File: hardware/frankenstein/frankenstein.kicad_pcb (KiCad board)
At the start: 2 copper layers, 100 x 99.9 mm, 259 parts, among them J351 MINI-USB-5P-3400020P1, M200 CONN_1, M201 CONN_1, M202 CONN_1, M351 CONN_1, M352 CONN_1, M401 CONN_1, M470 CONN_1, M471 CONN_1, P104 CONN_4, P201 CONN_10X2, P202 CONN_3, P203 CONN_2, P204 CONN_1, P205 CONN_1, P208 CONN_6, P209 CONN_6, P351 CONN_5X2, P352 MICRO-SDCARD-CONNECTOR-330006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, P353 CONN_10X2, P356 CONN_1, P401 CONN_3, P402 CONN_10X2, P403 CONN_16, P404 CONN_1, P405 CONN_1, P472 CONN_2, P51 CONN_4X2, P52 CONN_10X2, P53 CONN_2, P54 CONN_5X2, P55 CONN_6, P56 CONN_6, P57 CONN_6, P58 CONN_6, P603 CONN_6, P610 CONN_1, Q401 OVP_DRIVER, Q402 OVP_DRIVER, Q403 OVP_DRIVER, Q404 OVP_DRIVER, Q405 OVP_DRIVER, Q406 OVP_DRIVER, Q407 OVP_DRIVER, Q408 OVP_DRIVER, Q409 OVP_DRIVER, Q410 OVP_DRIVER, Q411 OVP_DRIVER, Q412 OVP_DRIVER, U101 MAX9926/9927, U201 LMV324IDR, U202 LMV324IDR, U203 LMV324IDR, U351 FT232RL, U471 SN65HVD230, U601 TC4427AVOA, U602 TC4427AVOA, U603 TC4427AVOA

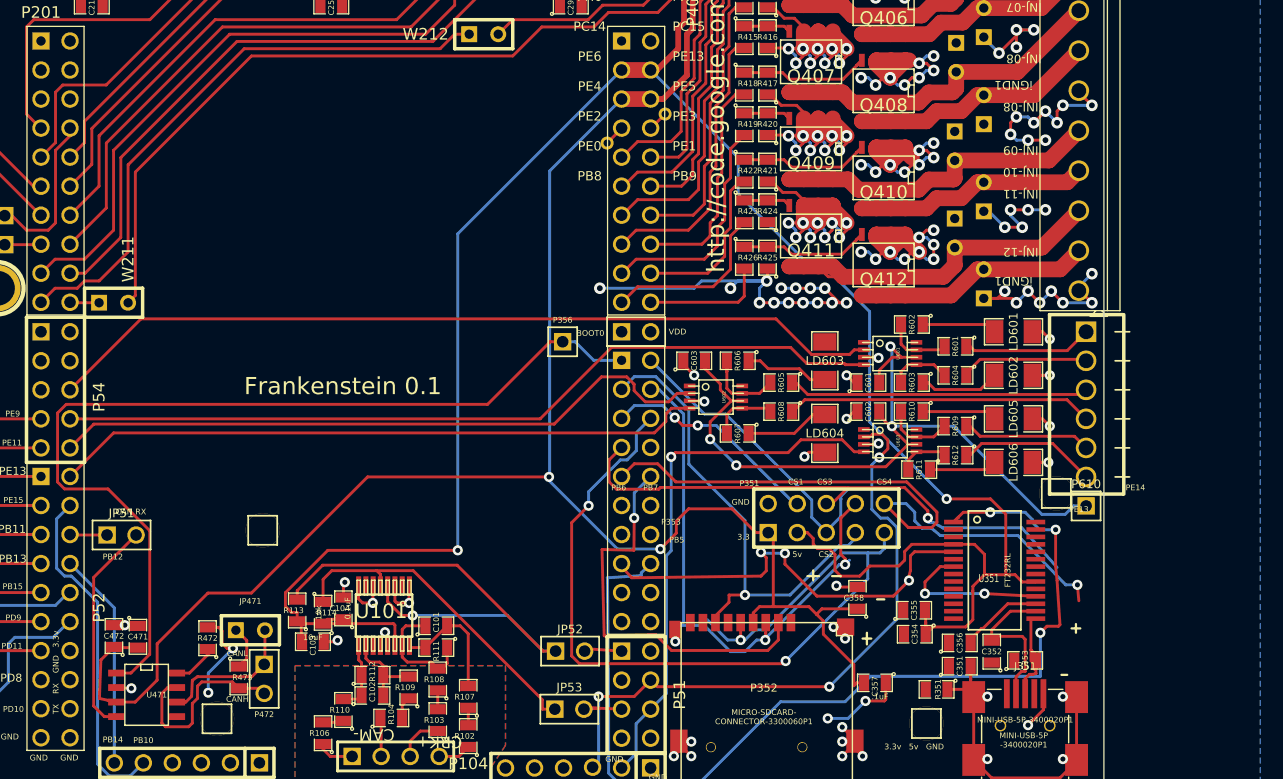
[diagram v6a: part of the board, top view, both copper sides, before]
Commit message: MSOP >> SOIC
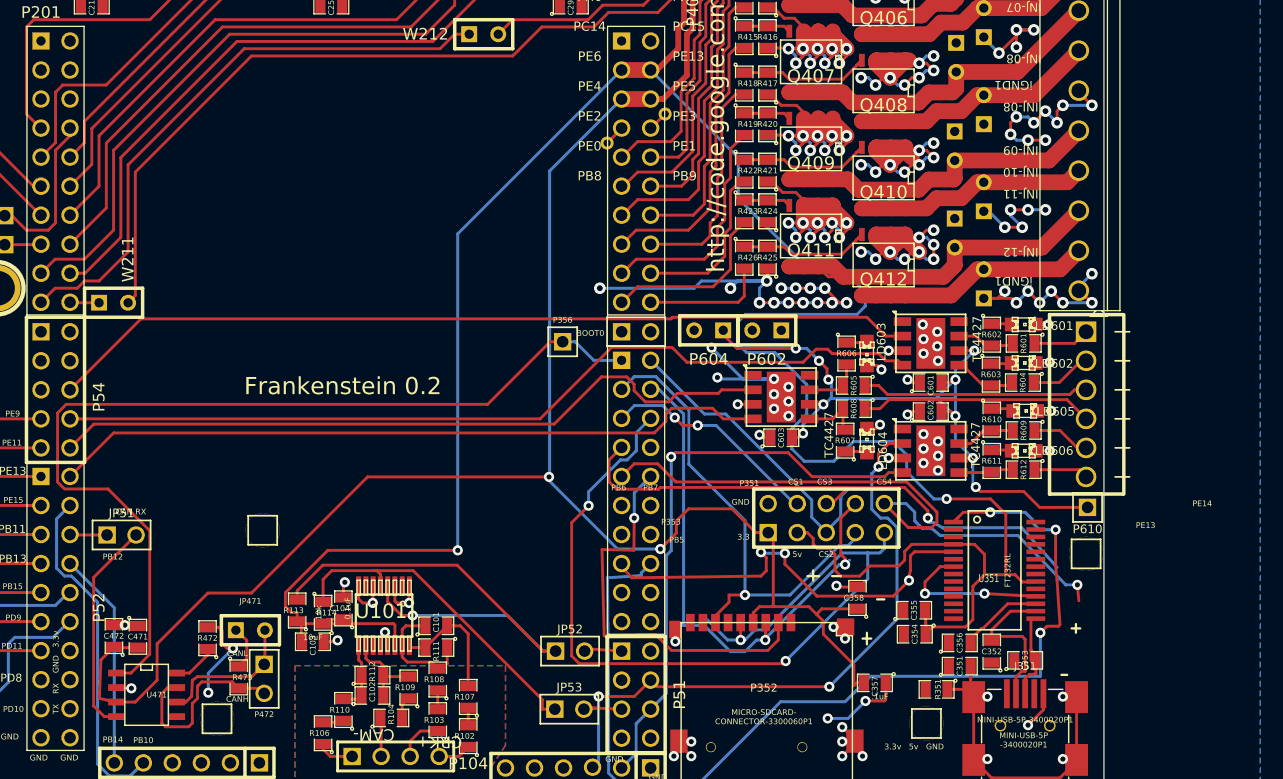
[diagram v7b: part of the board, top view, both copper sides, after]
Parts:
- added P602: CONN_2, SIL-2, F.Cu at (190.5, 152.3)
- added P604: CONN_2, SIL-2, F.Cu at (185.4, 152.3)
- LD601, LD602, LD603, LD604, LD605, LD606: footprint SM1206 -> LED-0805
- U601, U602, U603: value TC4427AVOA -> TC4427; footprint msoic-8 -> SOIC8-DFN
- moved G601 22.1 mm to (206.4, 160.0)
- moved C603 10.2 mm to (191.8, 161.7)
- moved R606 9.55 mm to (197.5, 154.3), turned to 270 degrees
- moved R607 9.42 mm to (197.4, 161.9), turned to 90 degrees
- moved R602 7.04 mm to (210.2, 152.7), turned to 270 degrees
- moved R610 7.02 mm to (210.2, 160.1), turned to 270 degrees
- moved R603 6.96 mm to (210.1, 156.1), turned to 270 degrees
- moved R611 6.40 mm to (210.2, 163.7), turned to 270 degrees
- moved R605 6.36 mm to (198.1, 157.1)
- moved R608 6.36 mm to (198.1, 159.1)
- moved R612 6.10 mm to (213.0, 164.5)
- moved R609 5.98 mm to (213.0, 161.0)
- moved R601 5.97 mm to (213.0, 153.4)
- moved R604 5.94 mm to (212.9, 156.8)
- moved M352 5.89 mm to (218.4, 171.8)
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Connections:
- net F-0000176 renamed N-0000020
- net F-0000177 renamed N-0000024
- net F-0000178 renamed N-000008
- net F-0000179 renamed N-0000025
- net F-0000180 renamed N-0000010
- net F-0000181 renamed N-0000021
- net F-0000182 renamed N-000001
- net F-0000183 renamed N-0000028
- net F-0000184 renamed N-0000012
- net F-0000185 renamed N-0000029
- net F-0000186 renamed N-000007
- net F-0000187 renamed N-000002
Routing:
- net GND: track 608.0 -> 663.0 mm, vias 264 -> 285
- net /5V: track 432.3 -> 458.4 mm
- net /HL6: track 12.1 -> 4.77 mm
- net /HL4: track 26.8 -> 20.4 mm
- net /HL1: track 11.3 -> 4.93 mm
- net /HL5: track 11.3 -> 5.14 mm
- net /H_IN4: track 57.1 -> 63.0 mm
- net /HL3: track 26.3 -> 20.4 mm
- net /HL2: track 11.3 -> 5.54 mm
- net /H_IN2: track 58.3 -> 64.0 mm
- net N-000008: track 7.35 -> 1.82 mm
- net N-000001: track 7.35 -> 1.94 mm
- net N-000002: track 7.05 -> 1.83 mm
- net N-0000010: track 6.55 -> 1.77 mm
- net N-000007: track 6.55 -> 1.95 mm
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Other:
- net class .02 added: clearance 0.1778, trace_width 0.508, via_dia 0.889, via_drill 0.635
- board text added: "Frankenstein 0.2"
- board text added: "P203"
- board text added: "R.02 https://code.google.com/p/daecu/"
- board text removed: "Frankenstein 0.1"
- board text removed: "VDD"
- board text removed: "https://code.google.com/p/daecu/ R.01"

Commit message: 0.11 not 0.2 yet
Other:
- board text added: "Frankenstein 0.11"
- board text removed: "Frankenstein 0.2"
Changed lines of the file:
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@@
       (xy 3.3401 -0.50546) (xy 3.34264 -0.09398) (xy 3.34518 -0.04318) (xy 3.34518 -0.04318)) (layer B.SilkS) (width 0.00254))
   )
-  (gr_text "Frankenstein 0.2" (at 153.416 157.1625) (layer B.SilkS)
+  (gr_text "Frankenstein 0.11" (at 153.416 157.1625) (layer B.SilkS)
     (effects (font (size 1.5 1.5) (thickness 0.3)) (justify mirror))
   )
-  (gr_text "Frankenstein 0.2" (at 153.416 157.1625) (layer F.SilkS)
+  (gr_text "Frankenstein 0.11" (at 153.416 157.1625) (layer F.SilkS)
     (effects (font (size 1.5 1.5) (thickness 0.3)))
   )
